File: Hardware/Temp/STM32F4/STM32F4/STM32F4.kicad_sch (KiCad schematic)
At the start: 29 parts, among them SW1 SW_Push, U1 STM32F407VET6, Y1 Crystal_8MHz_SMD-4PIN

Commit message: hardware:sche: update schematic F4, F1
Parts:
- removed R4: 10K/1%/1_10W, charge_battery_footprint_lib:Res_10K_0603, symbol charge_battery_sym_lib:Res_10K_0603_1%
- removed R6, R7: 0R/1%/1_10W, charge_battery_footprint_lib:Res_10K_0603, symbol charge_battery_sym_lib:Res_10K_0603_1%
- added C19: 10uF 16V, charge_battery_footprint_lib:Ceramic_Cap_10uF_16V, symbol charge_battery_sym_lib:Ceramic_Cap_SMD_10uF_16V
- added C20: 100nF 16V, charge_battery_footprint_lib:C_0603_1608Metric, symbol charge_battery_sym_lib:Ceramic_Cap_SMD_100nF_16V
- added J1: Conn_01x04_Pin, symbol Connector:Conn_01x04_Pin
- added JP1, JP2: Jumper_2_Small_Bridged, TestPoint:TestPoint_2Pads_Pitch2.54mm_Drill0.8mm, symbol Jumper:Jumper_2_Small_Bridged
- C1: value 1uF -> 1uF
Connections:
- net 3V3_FlyBack: no longer C10.2, C11.2, C12.2, C13.2, C6.2, C7.2, C8.2, C9.2, R1.1, R2.1, R3.2
- net GND2: now also C19.1, C20.1, J1.4 (Pin_4)
- net at R8.2: now also JP2.1 (A)
- net at R5.2: now also JP1.2 (B)
- net SWDIO: now reaches U1.72 (PA13)
- net SWDIO: now also J1.2 (Pin_2)
- net SWCLK: now reaches U1.76 (PA14)
- net SWCLK: now also J1.3 (Pin_3)
- net at U1.94 (BOOT0): now also JP2.2 (B)
- net BOOT1: no longer names the net of U1.37 (PB2)
- net BOOT1: now also JP1.1 (A)
- new net +3V3: C19.2, C20.2, J1.1 (Pin_1)
- new net 3V3: C10.2, C11.2, C12.2, C13.2, C6.2, C7.2, C8.2, C9.2, R1.1, R2.1, R3.2
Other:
- note added: "Chưa ra port cho các ngoại vi"
- note added: "LOAD PROGRAM"
- note removed: "BOOT1"
- note removed: "Chưa ra port cho các ngoại vi Chưa có chân nạp code"
- moved on the sheet: R5

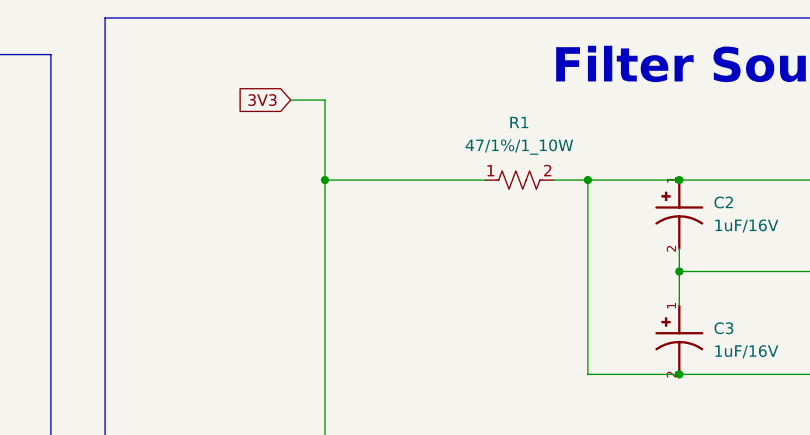
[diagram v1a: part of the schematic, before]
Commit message: Combine Sche in Source: PFC, LLC, F1, F4, ESP32
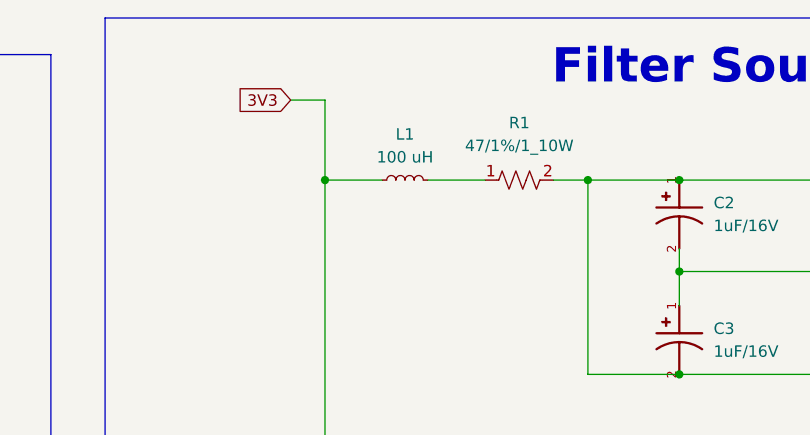
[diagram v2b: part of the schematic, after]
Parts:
- added L1: 100 uH, symbol Device:L_Small
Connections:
- net 3V3: now also L1.1; no longer R1.1
- new net: L1.2, R1.1
